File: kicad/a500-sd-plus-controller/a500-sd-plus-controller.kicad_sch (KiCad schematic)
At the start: 30 parts, among them J1 JTAG, J2 Conn_01x02, Q1 BSS138, U1 5M160ZE64, U2 SN74LVC4245A, U3 SN74LVC4245A, Y1 16MHz

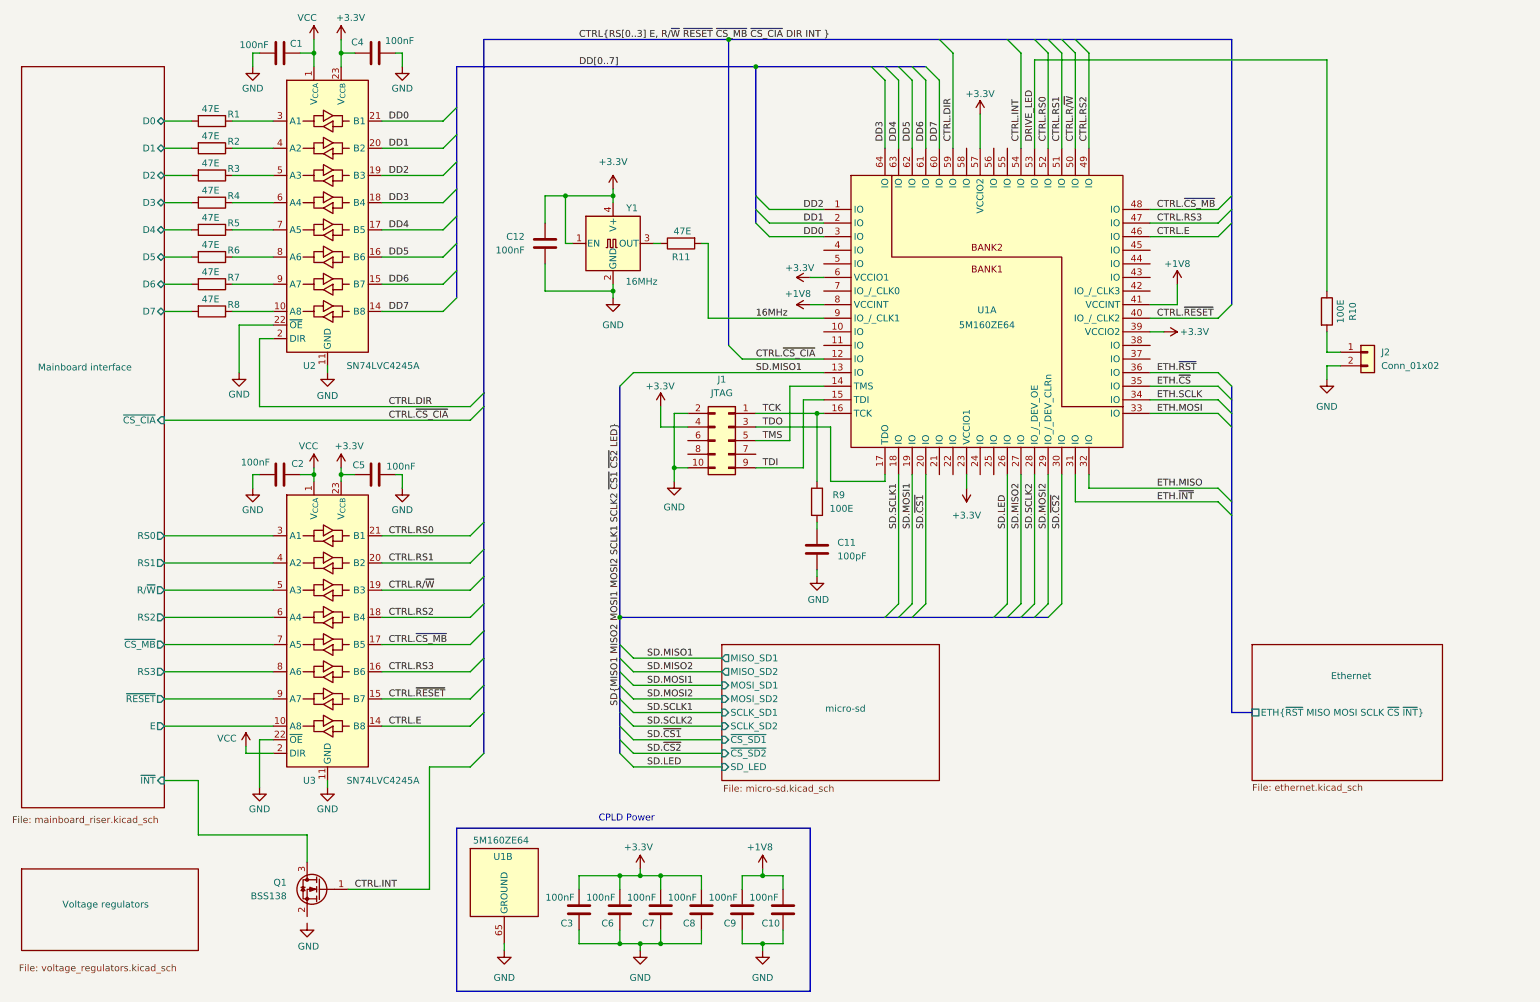
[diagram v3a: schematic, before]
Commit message: cleaned up silkscreen and 3D models
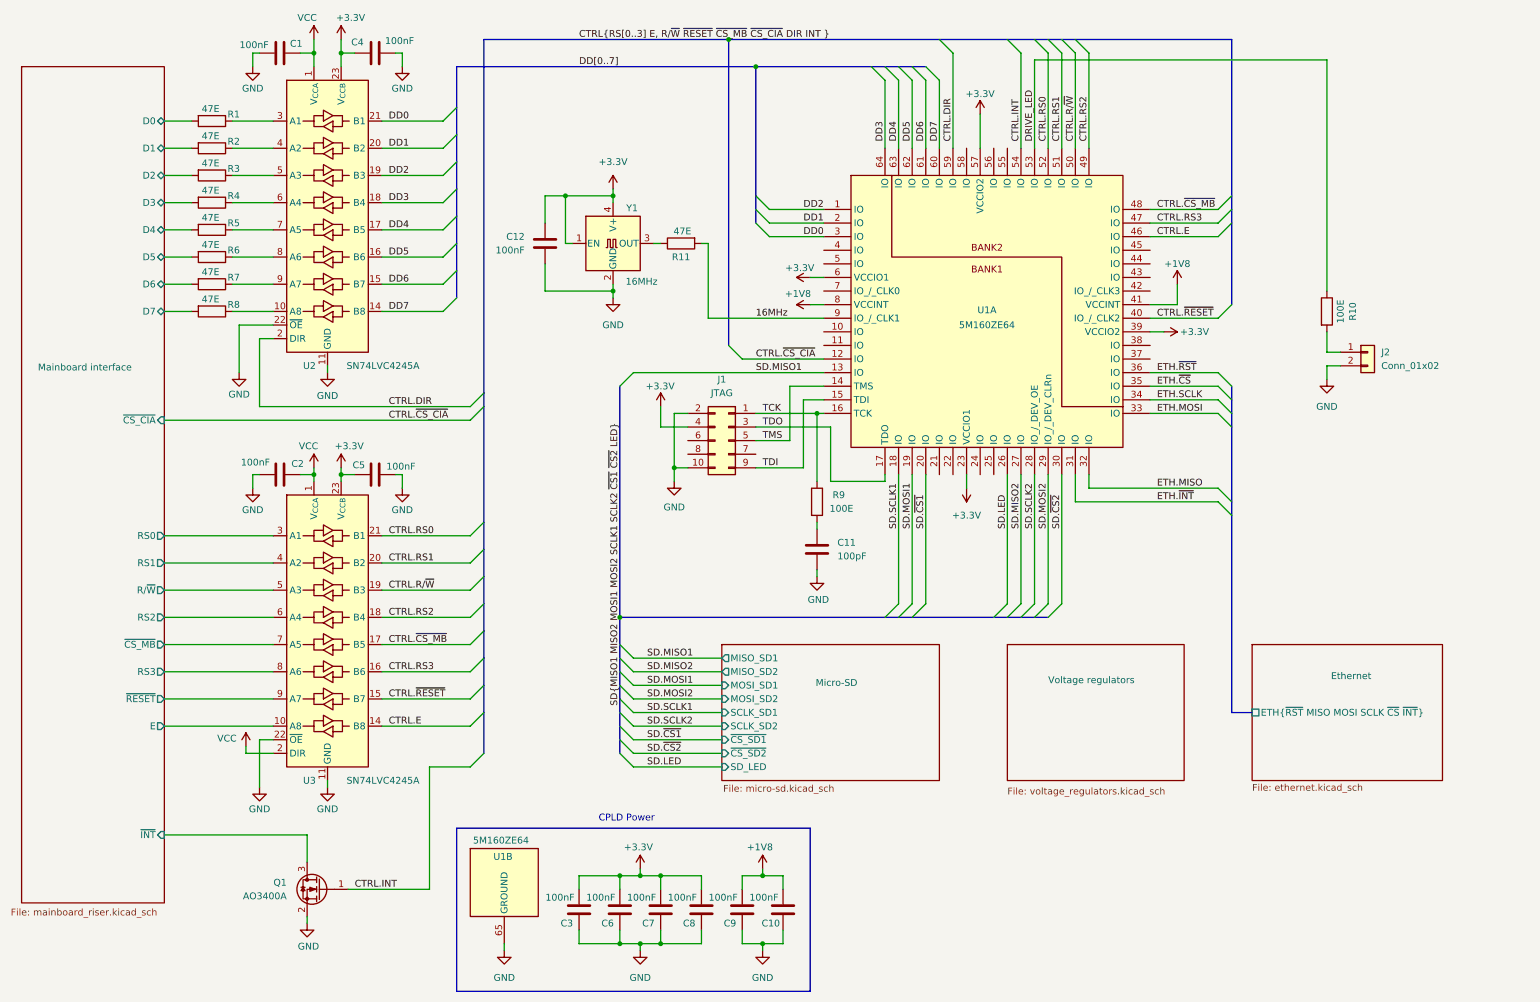
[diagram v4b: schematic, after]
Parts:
- Q1: value BSS138 -> AO3400A
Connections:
- net GND: now also Q1.2 (S)
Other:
- sheet micro-sd renamed Micro-SD
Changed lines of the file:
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@@
 	(wire
 		(pts
+			(xy 71.12 182.88) (xy 71.12 184.15)
+		)
+		(stroke
+			(width 0)
+			(type default)
+		)
+	)
+	(wire
+		(pts
 			(xy 85.09 59.69) (xy 96.52 59.69)
 		)
@@
 	(wire
 		(pts
-			(xy 50.8 157.48) (xy 44.45 157.48)
+			(xy 44.45 167.64) (xy 71.12 167.64)
 		)
 		(stroke
@@
 	(wire
 		(pts
-			(xy 50.8 167.64) (xy 50.8 157.48)
-		)
-		(stroke
-			(width 0)
-			(type default)
-		)
-	)
-	(wire
-		(pts
 			(xy 44.45 116.84) (xy 64.77 116.84)
 		)
@@
 	(wire
 		(pts
-			(xy 71.12 167.64) (xy 50.8 167.64)
-		)
-		(stroke
-			(width 0)
-			(type default)
-		)
-	)
-	(wire
-		(pts
 			(xy 168.91 91.44) (xy 154.94 91.44)
 		)
@@
 			)
 		)
-		(property "Value" "BSS138"
+		(property "Value" "AO3400A"
 			(at 67.31 179.0699 0)
 			(effects
@@
 	)
 	(sheet
-		(at 17.78 173.99)
-		(size 33.02 15.24)
+		(at 201.93 132.08)
+		(size 33.02 25.4)
 		(exclude_from_sim no)
 		(in_bom yes)
@@
 		)
 		(property "Sheetname" "Voltage regulators"
-			(at 25.4 181.356 0)
+			(at 209.55 139.446 0)
 			(effects
 				(font
@@
 		)
 		(property "Sheetfile" "voltage_regulators.kicad_sch"
-			(at 17.272 191.77 0)
+			(at 201.93 158.75 0)
 			(effects
 				(font
@@
 			(color 255 255 194 1.0000)
 		)
-		(property "Sheetname" "micro-sd"
-			(at 167.894 144.78 0)
+		(property "Sheetname" "Micro-SD"
+			(at 166.116 139.954 0)
 			(effects
 				(font
@@
 	(sheet
 		(at 17.78 24.13)
-		(size 26.67 138.43)
+		(size 26.67 156.21)
 		(exclude_from_sim no)
 		(in_bom yes)
@@
 		)
 		(property "Sheetfile" "mainboard_riser.kicad_sch"
-			(at 16.002 164.084 0)
+			(at 15.748 181.356 0)
 			(effects
 				(font
@@
 		)
 		(pin "~{INT}" input
-			(at 44.45 157.48 0)
+			(at 44.45 167.64 0)
 			(effects
 				(font

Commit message: PCB done, this version has been sent to fabrication
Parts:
- C1, C10, C12, C2, C3, C4, C5, C6, C7, C8, C9: LCSC Part # (none) -> C14663; Quantity (none) -> ${QUANTITY}
- C11: LCSC Part # (none) -> C14858; Quantity (none) -> ${QUANTITY}
- J1, J2: Quantity (none) -> ${QUANTITY}
- Q1: LCSC Part # (none) -> C20917; MPN (none) -> AO3400A; Quantity (none) -> ${QUANTITY}
- R1, R11, R2, R3, R4, R5, R6, R7, R8: value 47E -> 100R; LCSC Part # (none) -> C22775; Quantity (none) -> ${QUANTITY}
- R10: value 100E -> 470R; LCSC Part # (none) -> C23179; Quantity (none) -> ${QUANTITY}
- R9: value 100E -> 100R; LCSC Part # (none) -> C22775; Quantity (none) -> ${QUANTITY}
- U1: LCSC Part # (none) -> C431489; MPN 5M160ZE64I5N -> 5M160ZE64C5N; Quantity (none) -> ${QUANTITY}
- U2, U3: LCSC Part # (none) -> C7859; Quantity (none) -> ${QUANTITY}
- Y1: LCSC Part # (none) -> C255993; Quantity (none) -> ${QUANTITY}
